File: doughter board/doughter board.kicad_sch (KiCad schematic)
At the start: 38 parts, among them J3 Conn_01x05, J301 RS485, J305 BOOT_TO/ SELECTOR, J306 UART2, J310 Serial_BUS, J311 BOOT_TO/ SELECTOR, J5 OUTPUT, SW301 SW_SPST, U301 SN65HVD11, U302 LM1117-3.3, U303 STM32F030C6Tx, Y301 8 MHz

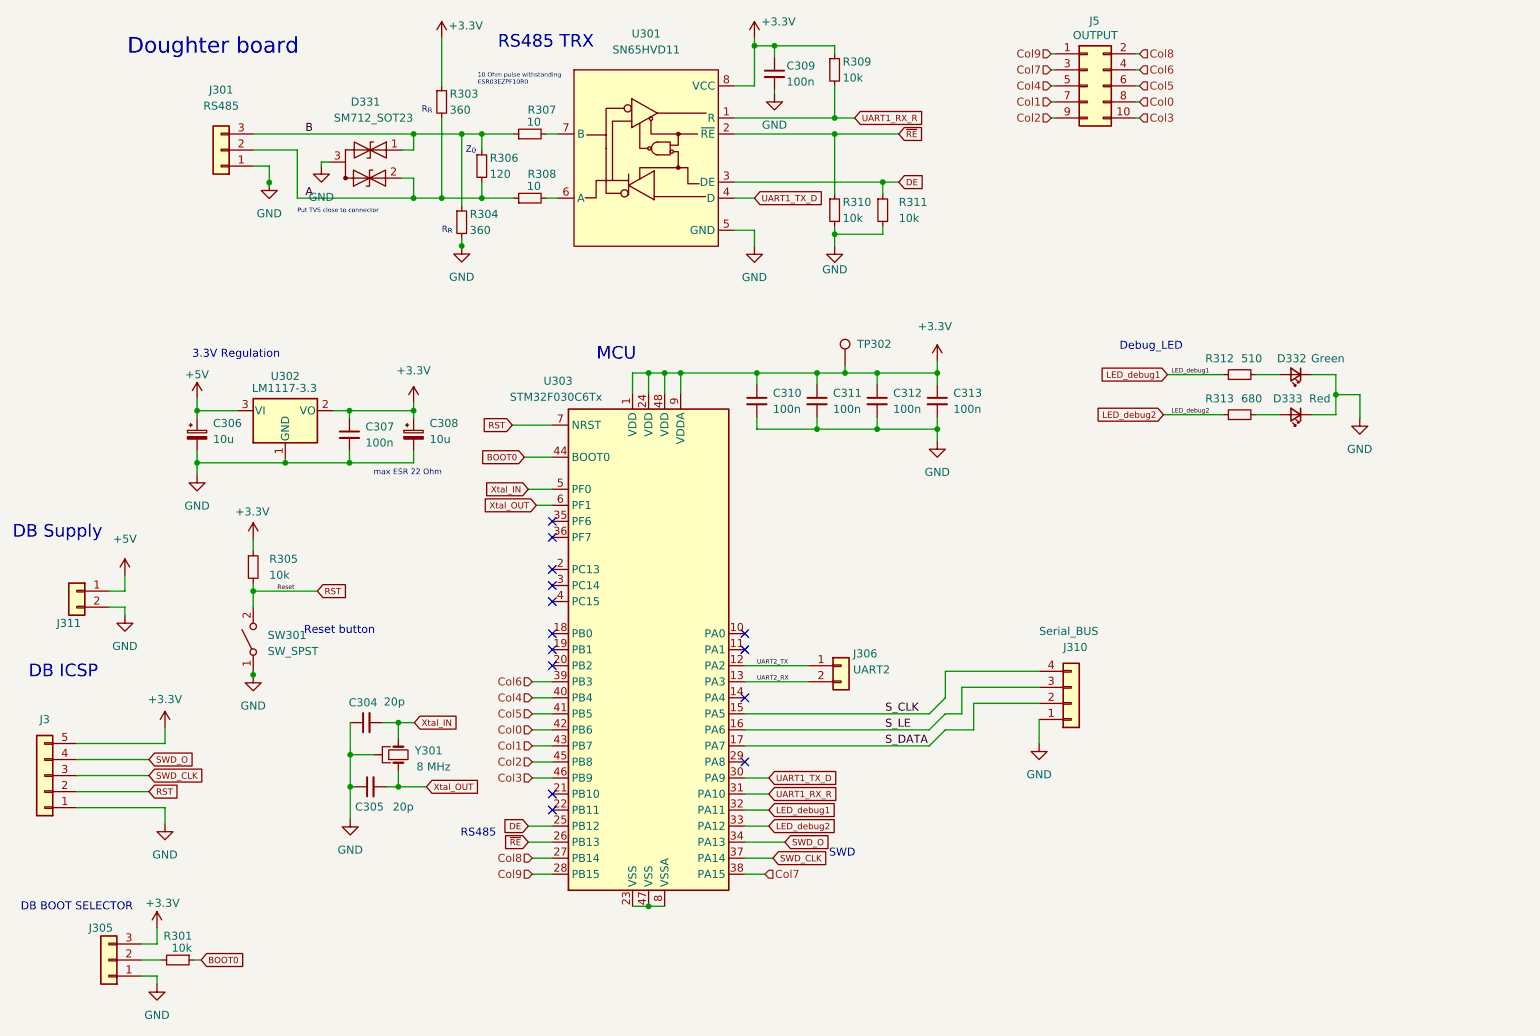
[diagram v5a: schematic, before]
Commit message: finished pcb, except copper slab
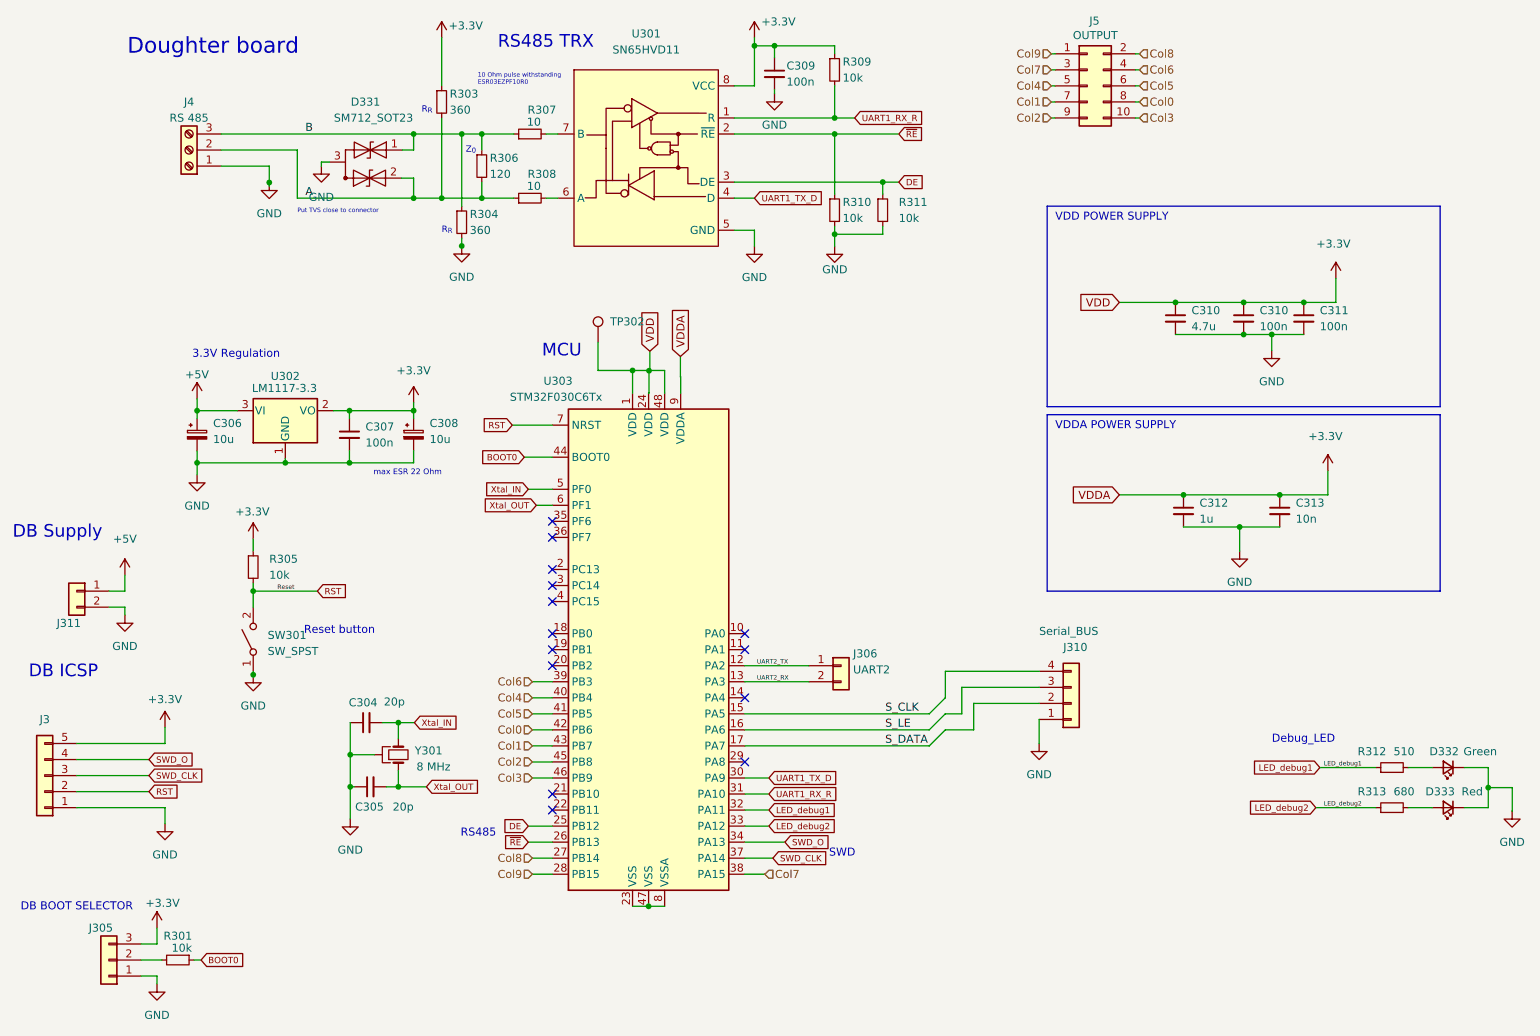
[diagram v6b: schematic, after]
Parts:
- removed J301: RS485, Connector_PinSocket_2.54mm:PinSocket_1x03_P2.54mm_Vertical_SMD_Pin1Right, symbol Connector_Generic:Conn_01x03
- added C310: 4.7u, Capacitor_SMD:C_0603_1608Metric_Pad1.08x0.95mm_HandSolder, symbol Device:C_Small
- added J4: RS 485, TerminalBlock_Altech:Altech_AK300_1x03_P5.00mm_45-Degree, symbol Connector:Screw_Terminal_01x03
- C312: value 100n -> 1u
- C313: value 100n -> 10n
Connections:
- net +3.3V: now also C310.1; no longer TP302.1, U303.1 (VDD), U303.48 (VDD)
- net A: now also J4.2 (Pin_2)
- net B: now also J4.3 (Pin_3)
- net GND: now also C310.2, J4.1 (Pin_1)
- new net: TP302.1, U303.1 (VDD), U303.48 (VDD)
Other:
- note added: "VDD POWER SUPPLY"
- note added: "VDDA POWER SUPPLY"
- moved on the sheet: C310, C311, C312, C313, D332, D333, R312, R313, TP302
